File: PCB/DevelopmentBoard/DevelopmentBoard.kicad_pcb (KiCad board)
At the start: 2 copper layers, 152.4 x 76.2 mm, 26 parts, among them J2 Conn_01x04_MountingPin-Payloa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, J5 Conn_01x04_MountingPin, U1 D24V22F5_VoltageRegulator, U2 Barometer_Grove, U3 RASPBERRY_PI_3_MODEL_B+, U4 Conn_01x08_DevBoardSymbols, U6 MCP3008_ADC, U7 Conn_01x06_DevBoard_Symbols, X1 XT30, X2 XT30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

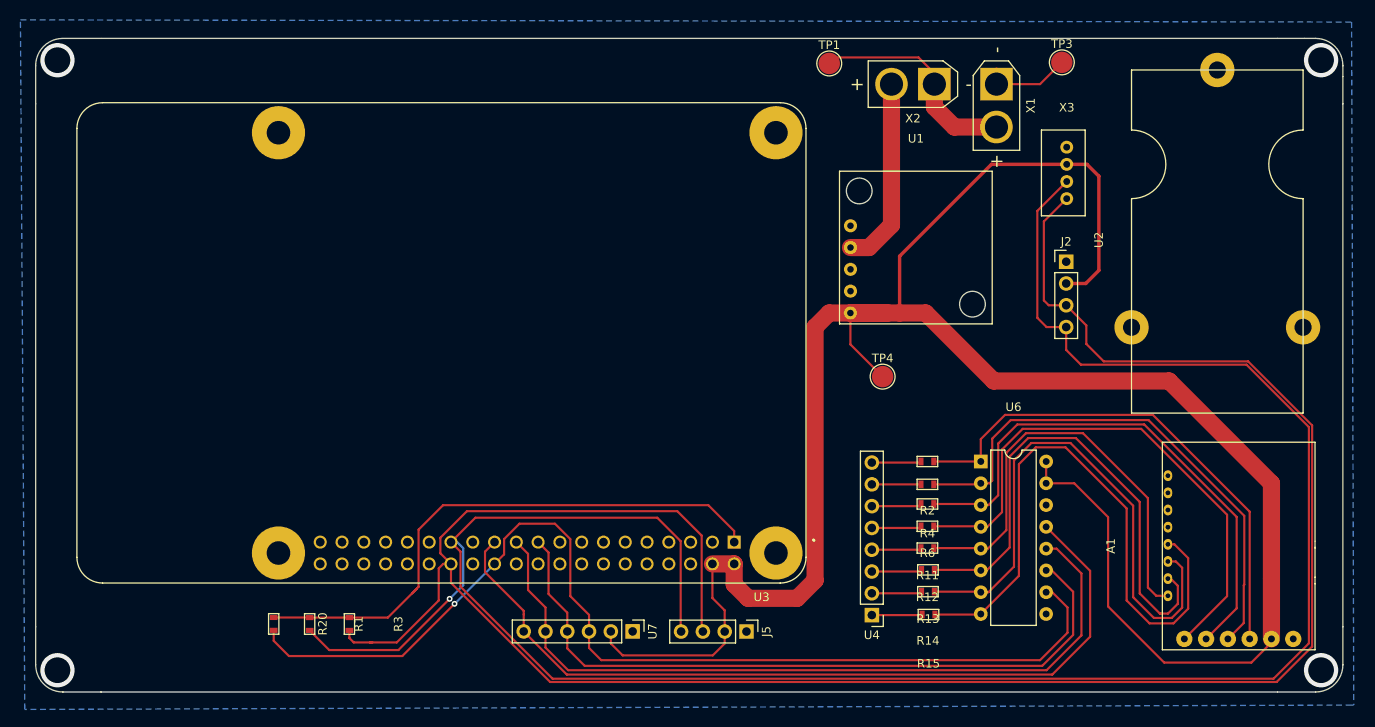
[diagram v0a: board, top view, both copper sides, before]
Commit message: Added 3.3V testpoint
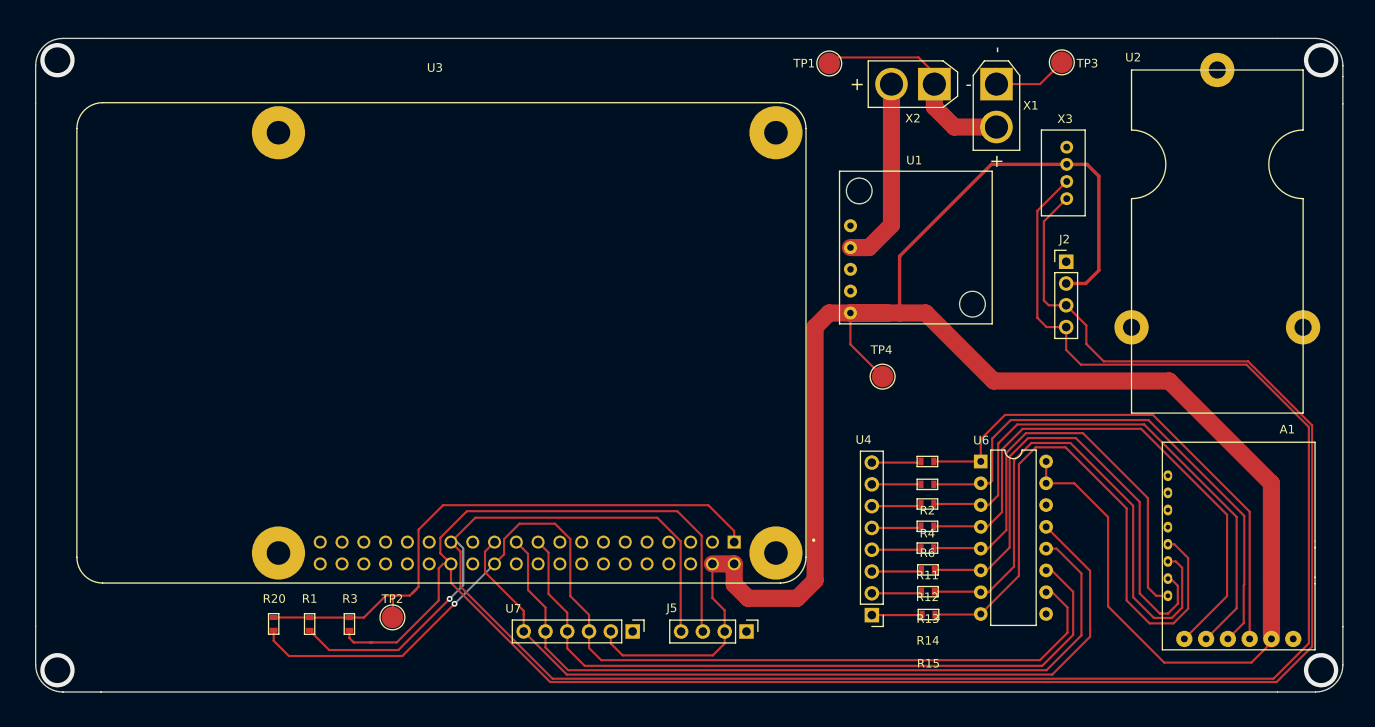
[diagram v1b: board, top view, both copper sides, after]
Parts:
- added TP2: TestPoint, TestPoint:TestPoint_Pad_D2.5mm, F.Cu at (114.3, 129.9)
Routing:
- net +3V3: track 66.7 -> 69.3 mm
- removed copper zone on B.Cu, net GND

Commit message: Rewired I2C Pins on the Pi
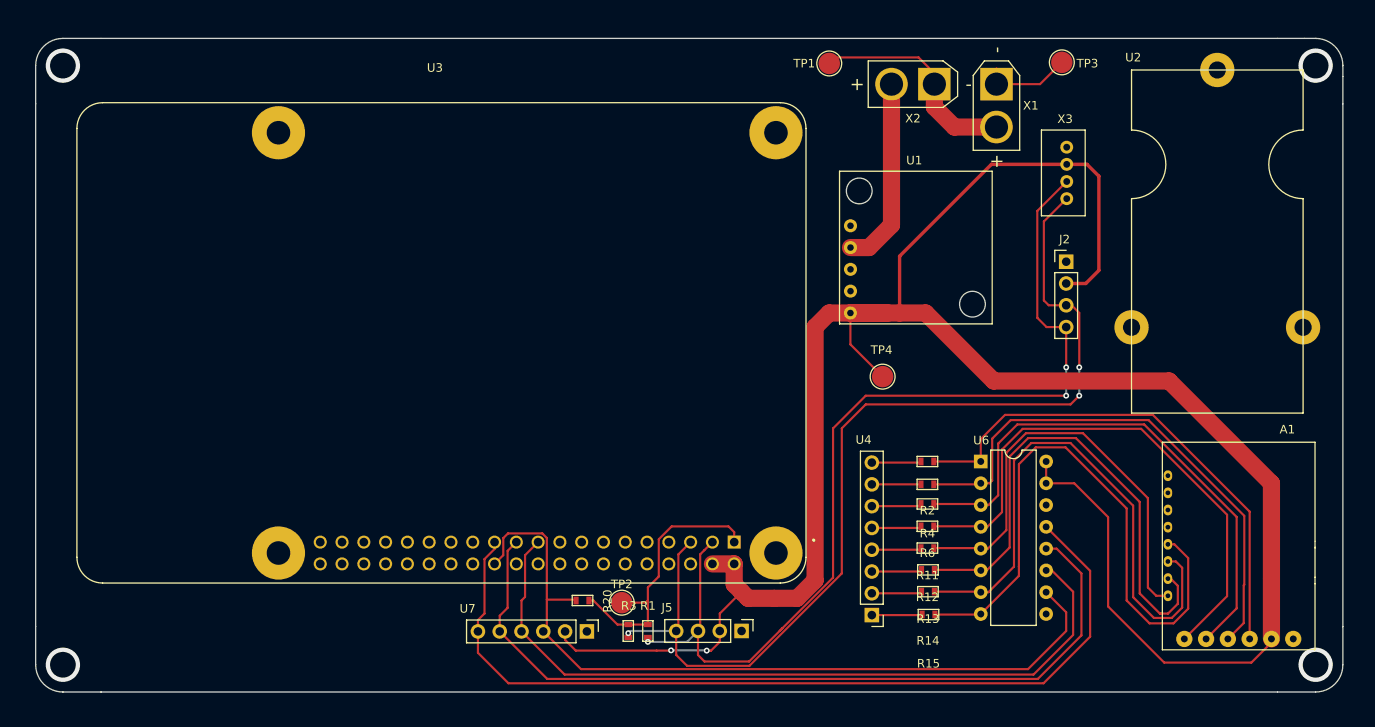
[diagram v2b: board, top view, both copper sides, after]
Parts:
- moved R1 39.4 mm to (144.1, 131.5)
- moved R20 36.1 mm to (136.5, 128.0), turned to 180 degrees
- moved R3 32.5 mm to (141.8, 131.5)
- moved TP2 26.8 mm to (141.0, 128.2)
- moved U7 5.33 mm to (137.0, 131.6)
- moved J5 0.58 mm to (155.0, 131.5)
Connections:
- J5 pad 3: /SCL -> /SDA
- J5 pad 4: /SDA -> /SCL
- U3 pad 27: /SDA -> Net-(U3-Pad27)
- U3 pad 28: /SCL -> Net-(U3-Pad28)
- U3 pad 3: Net-(U3-Pad3) -> /SDA
- U3 pad 5: Net-(U3-Pad5) -> /SCL
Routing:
- net /SDA: track 260.1 -> 116.6 mm, vias 1 -> 3
- net /SCL: track 253.4 -> 117.9 mm, vias 0 -> 3
- net +3V3: track 69.3 -> 32.5 mm
- net /CS_ADC: track 122.2 -> 93.6 mm, vias 1 -> 0
- net /SCLK: track 97.6 -> 103.7 mm
- net /MOSI: track 84.4 -> 89.4 mm
- net /MISO: track 91.5 -> 96.0 mm
- net +5V: track 260.2 -> 262.6 mm, vias 0 -> 2

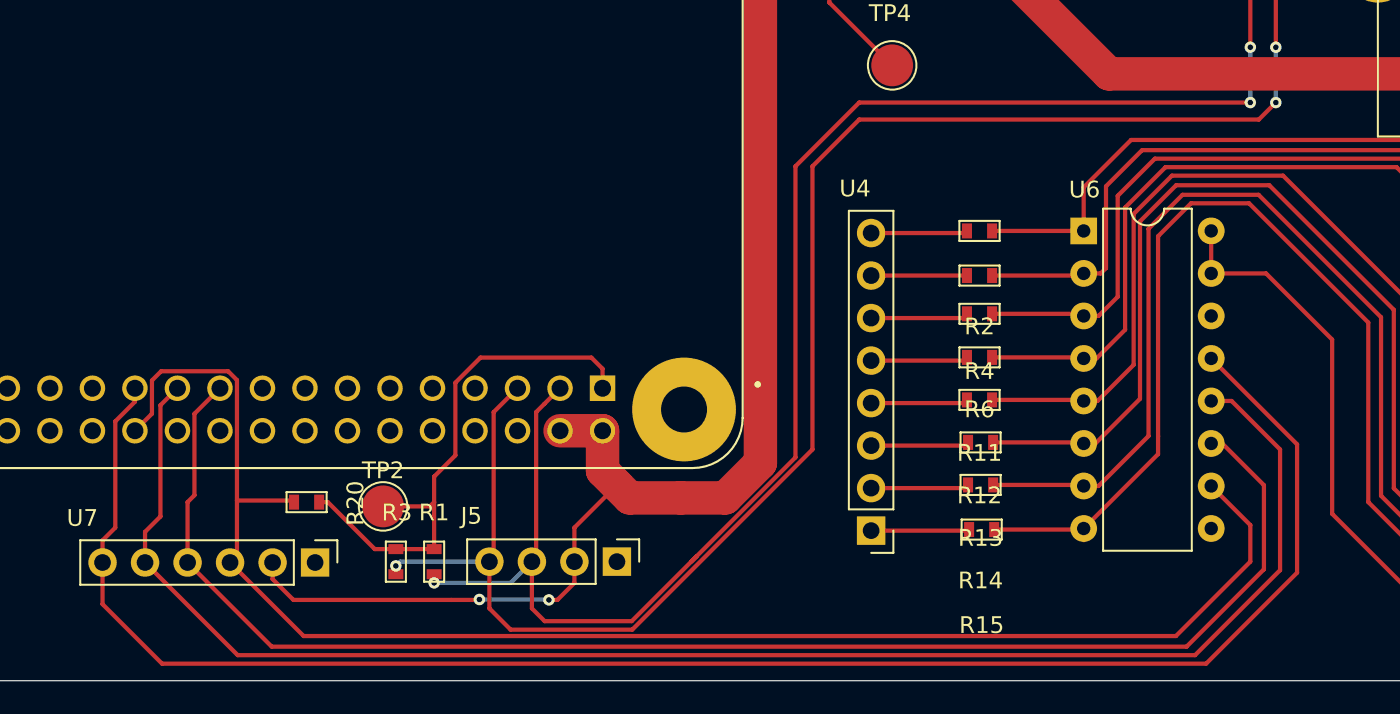
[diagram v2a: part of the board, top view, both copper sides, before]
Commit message: Adjusted traces.
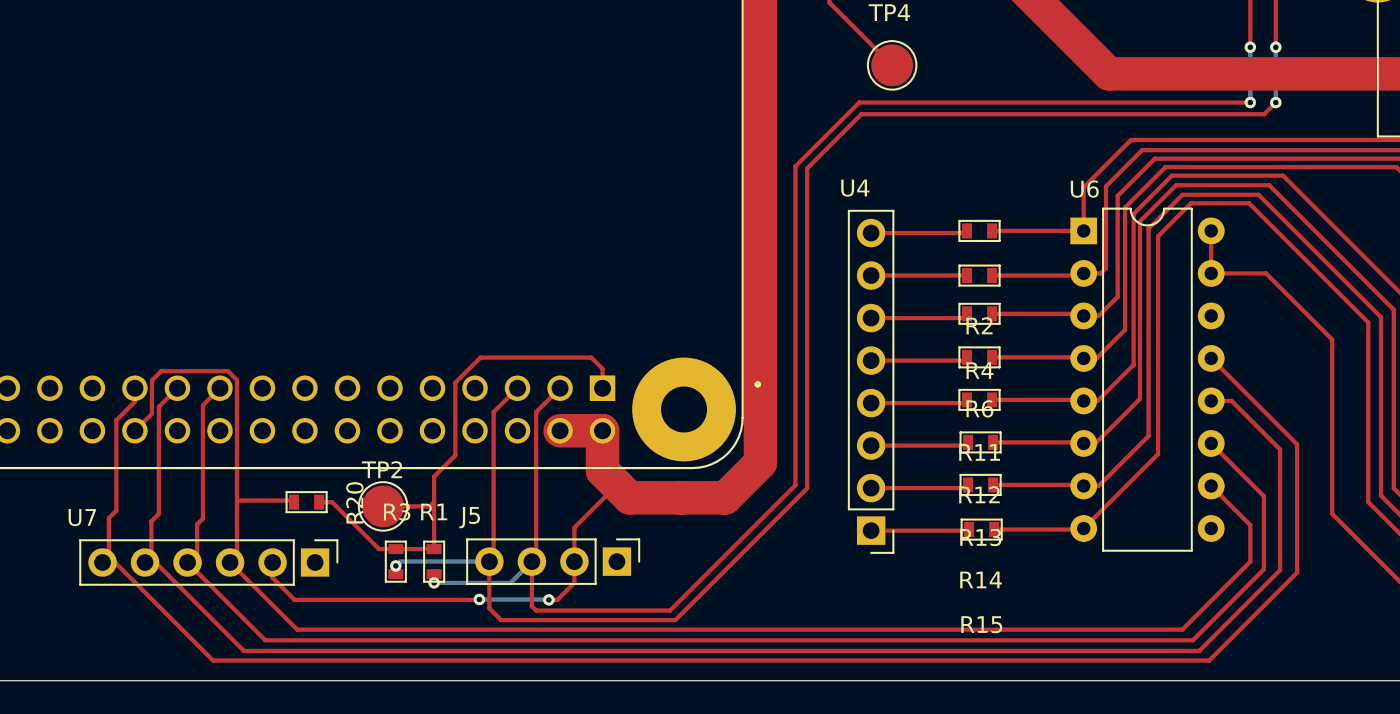
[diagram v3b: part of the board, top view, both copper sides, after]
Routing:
- net /SCLK: track 103.7 -> 102.1 mm
- net /SCL: track 117.9 -> 118.7 mm
- net /MOSI: track 89.4 -> 88.7 mm

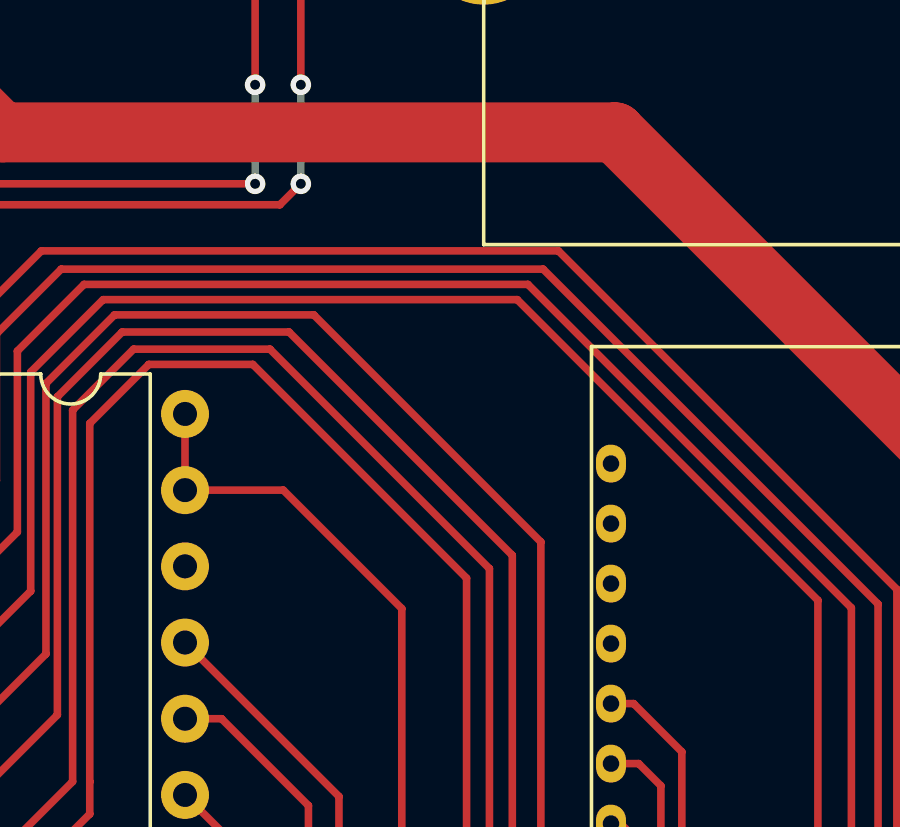
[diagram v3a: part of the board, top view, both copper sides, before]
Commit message: Added I2C Outputs on the TBS Module
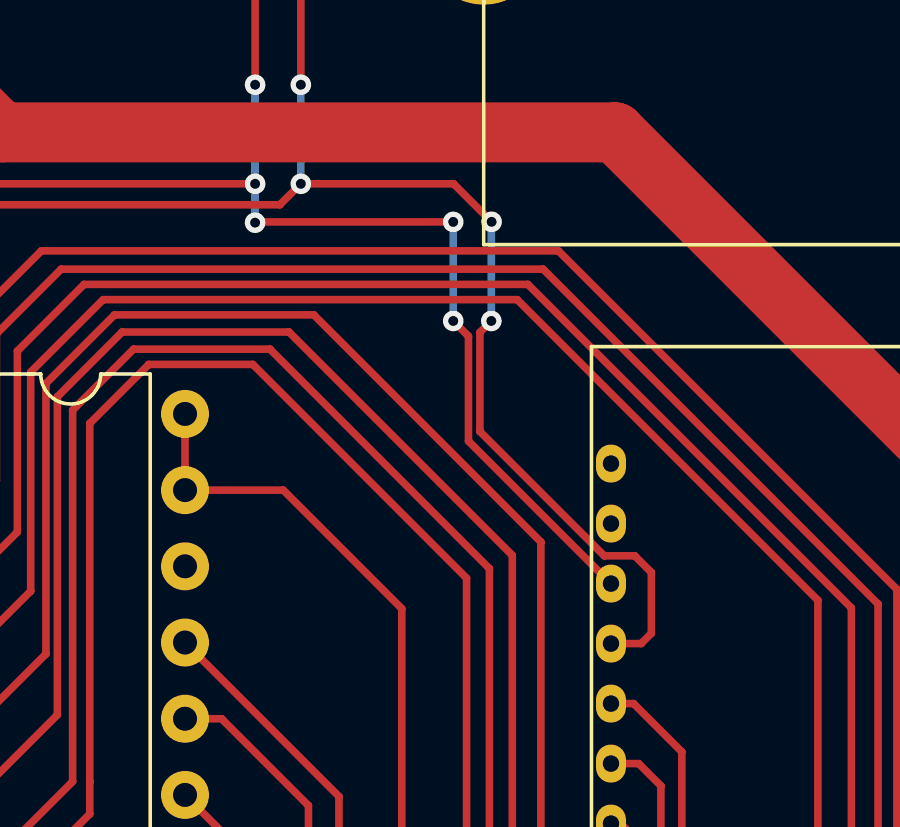
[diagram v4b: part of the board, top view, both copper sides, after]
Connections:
- A1 pad 11: Net-(A1-Pad11) -> /SCL
- A1 pad 12: Net-(A1-Pad12) -> /SDA
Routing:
- net /SCL: track 118.7 -> 143.9 mm, vias 3 -> 5
- net /SDA: track 116.5 -> 138.6 mm, vias 3 -> 6

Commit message: FInal Tracing changes and Copper Refill.
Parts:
- added G***: LOGO, DevelopmentBoard:PayloadLogo, F.Cu at (83.2, 132.2)
- moved TP1 1.37 mm to (166.5, 64.9)
- renumbered R20 to R5
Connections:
- TP1 pad 1: +12V -> Net-(TP1-Pad1)
- U1 pad 2: Net-(U1-Pad2) -> Net-(TP1-Pad1)
- X2 pad 2: Net-(U1-Pad2) -> Net-(TP1-Pad1)
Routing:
- net Net-(TP1-Pad1): track 0.00 -> 35.2 mm
- net Net-(U1-Pad2): track 22.3 -> 0.00 mm
- net +12V: track 25.4 -> 12.1 mm
- added copper zone on B.Cu, net GND
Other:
- board text added: "ADC"
- board text added: "Altimeter"
- board text added: "Raspberry PI"
- board text added: "Receiver"
- board text added: "Regulator"

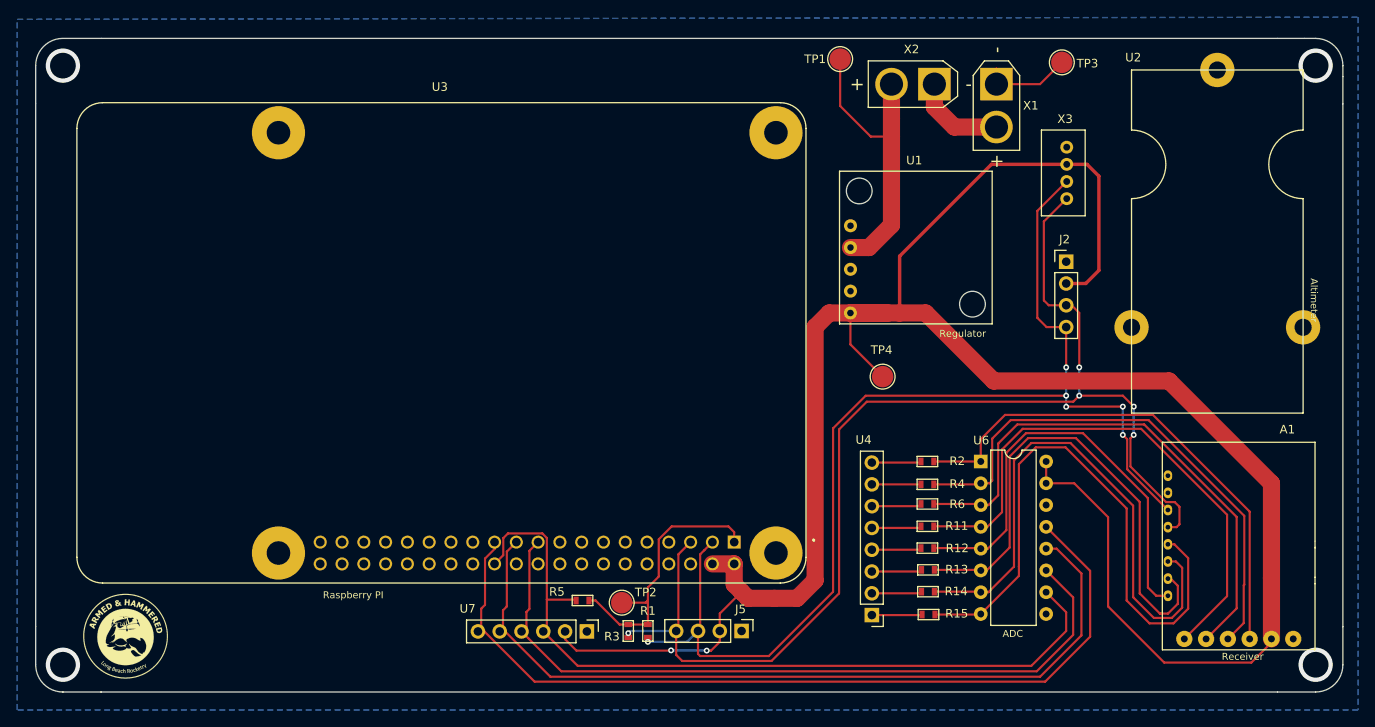
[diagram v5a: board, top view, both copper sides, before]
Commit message: Adjusted some traces and silkscreen locations
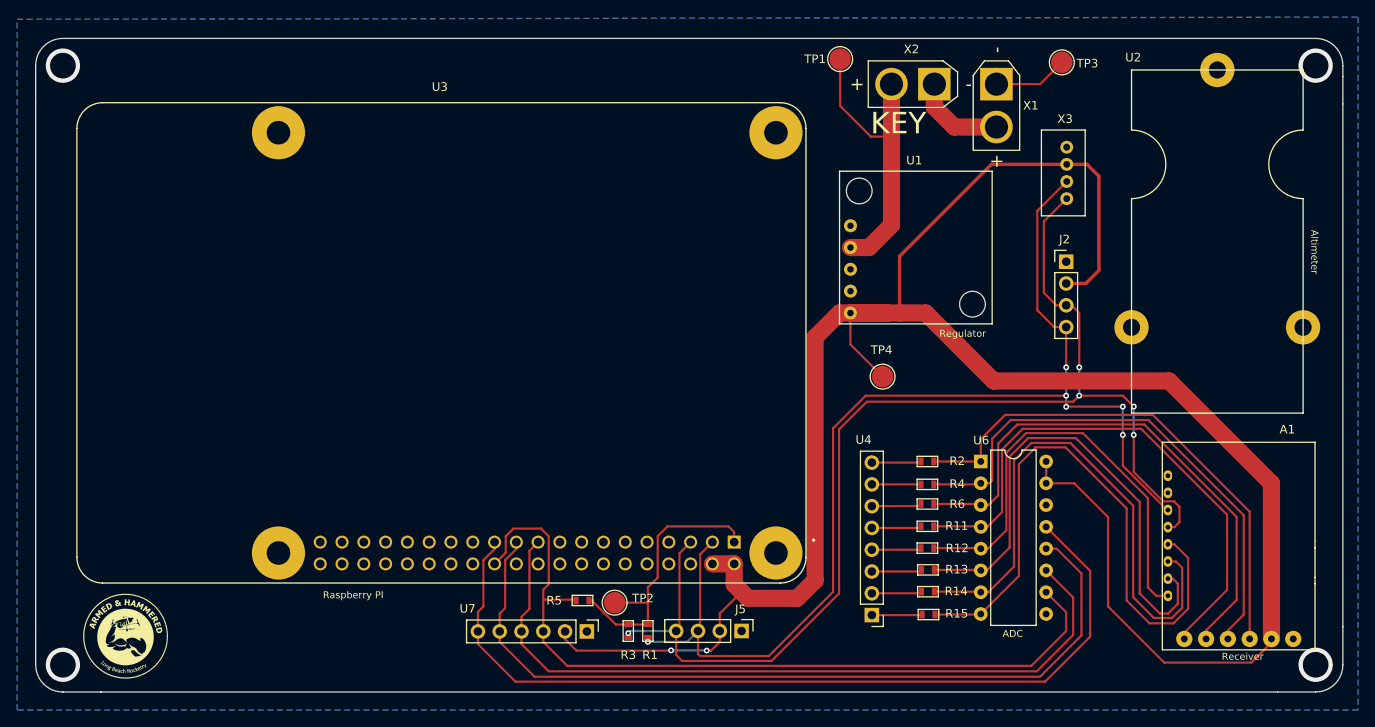
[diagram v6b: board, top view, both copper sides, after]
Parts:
- moved TP2 0.83 mm to (140.2, 128.2)
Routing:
- net /CS_ADC: track 93.3 -> 95.2 mm
- net /SCLK: track 102.1 -> 103.0 mm
- net /MOSI: track 88.7 -> 89.6 mm
- net /SCL: track 143.9 -> 143.1 mm
- net /MISO: track 95.7 -> 96.5 mm
- net +5V: track 262.6 -> 261.9 mm
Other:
- board text added: "KEY"

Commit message: added snek footprint file
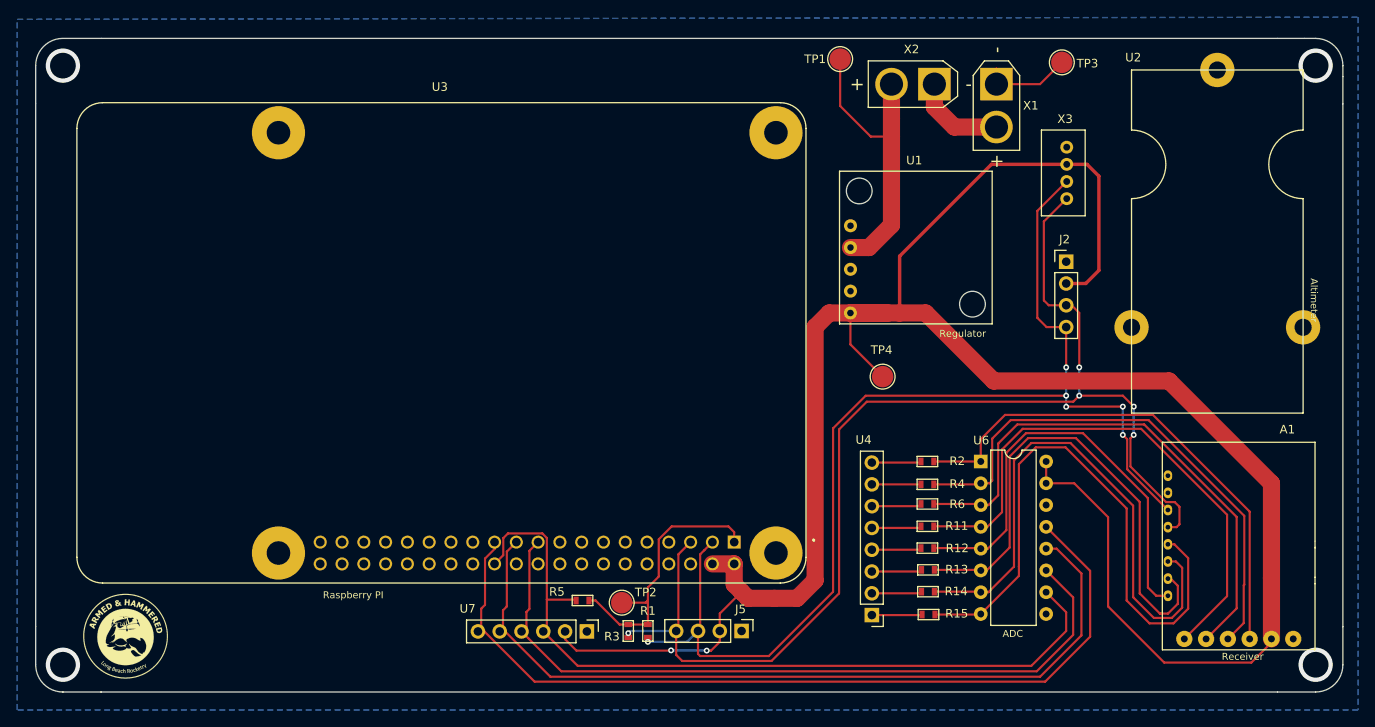
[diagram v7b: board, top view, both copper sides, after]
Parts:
- moved TP2 0.83 mm to (141.0, 128.2)
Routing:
- net /CS_ADC: track 95.2 -> 93.3 mm
- net /SCLK: track 103.0 -> 102.1 mm
- net /MOSI: track 89.6 -> 88.7 mm
- net /SCL: track 143.1 -> 143.9 mm
- net /MISO: track 96.5 -> 95.7 mm
- net +5V: track 261.9 -> 262.6 mm
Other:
- board text removed: "KEY"

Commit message: Added front and back silk screen.
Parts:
- added G***: LOGO, DevelopmentBoard:Snek, B.Cu at (147.3, 100.4)
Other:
- board text added: "Created By: - Allan Flores - Josias Navasca "Do it with passion or don't do it at all""
